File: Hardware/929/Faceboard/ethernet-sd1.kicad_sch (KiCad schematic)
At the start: 13 parts, among them J2 Raspberry_Pi_to_Ziloo, J4 RJ45_LED_Shielded

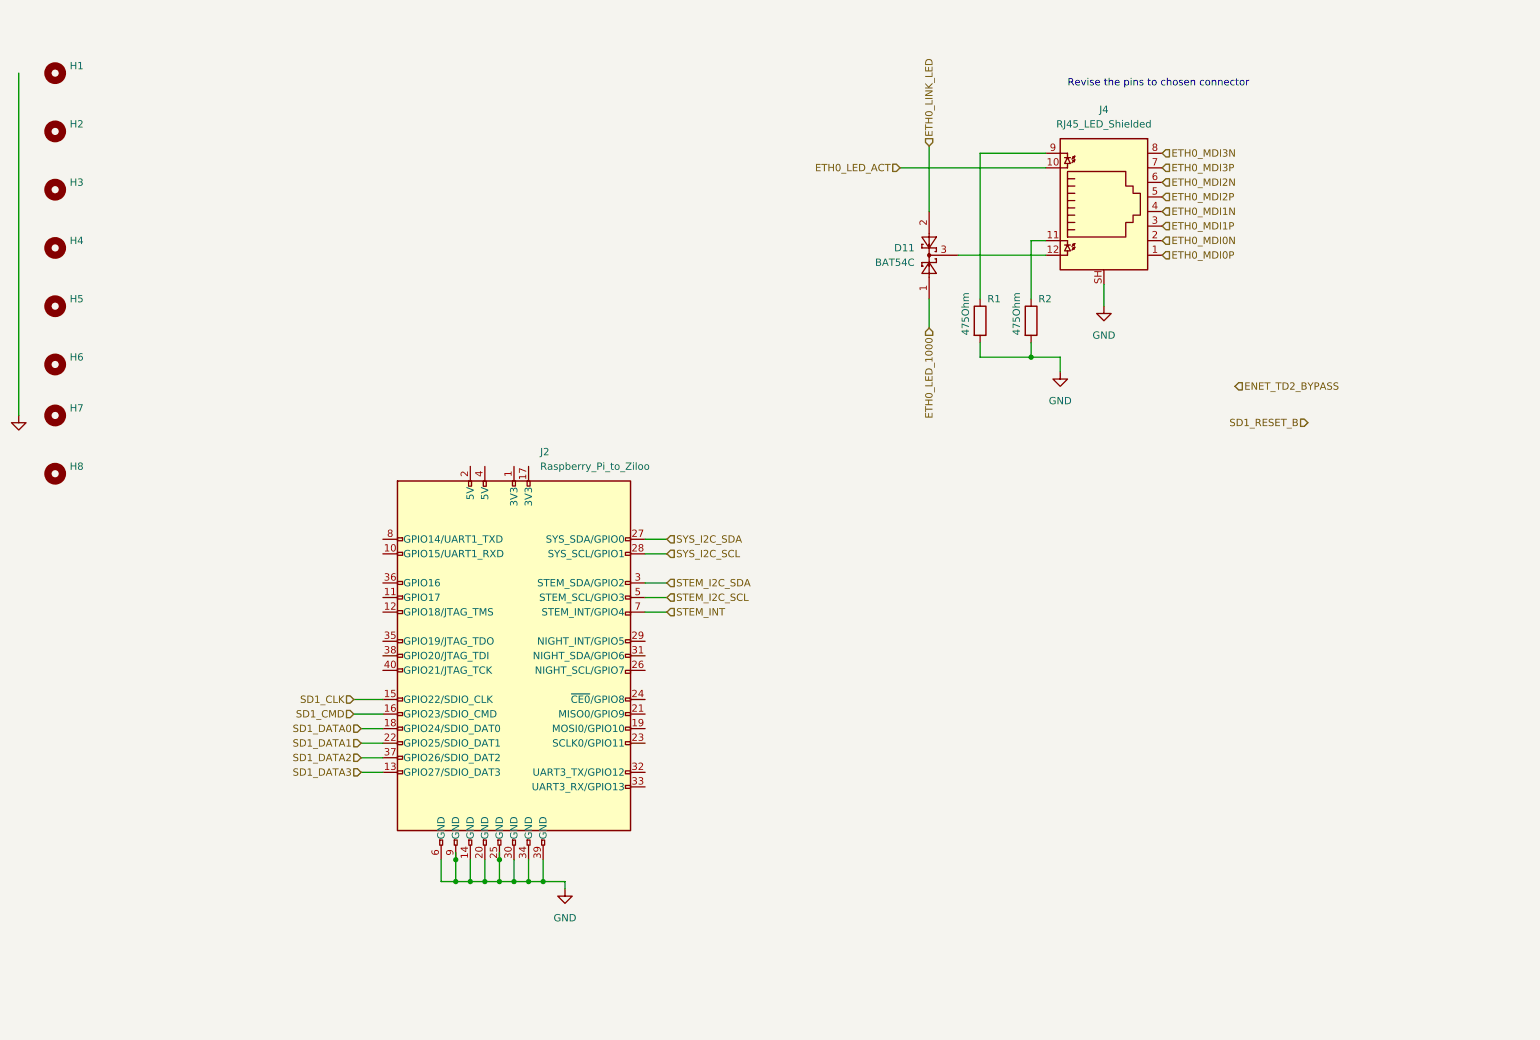
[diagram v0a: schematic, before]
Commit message: Added components
ESD HDMI
Extra components planned
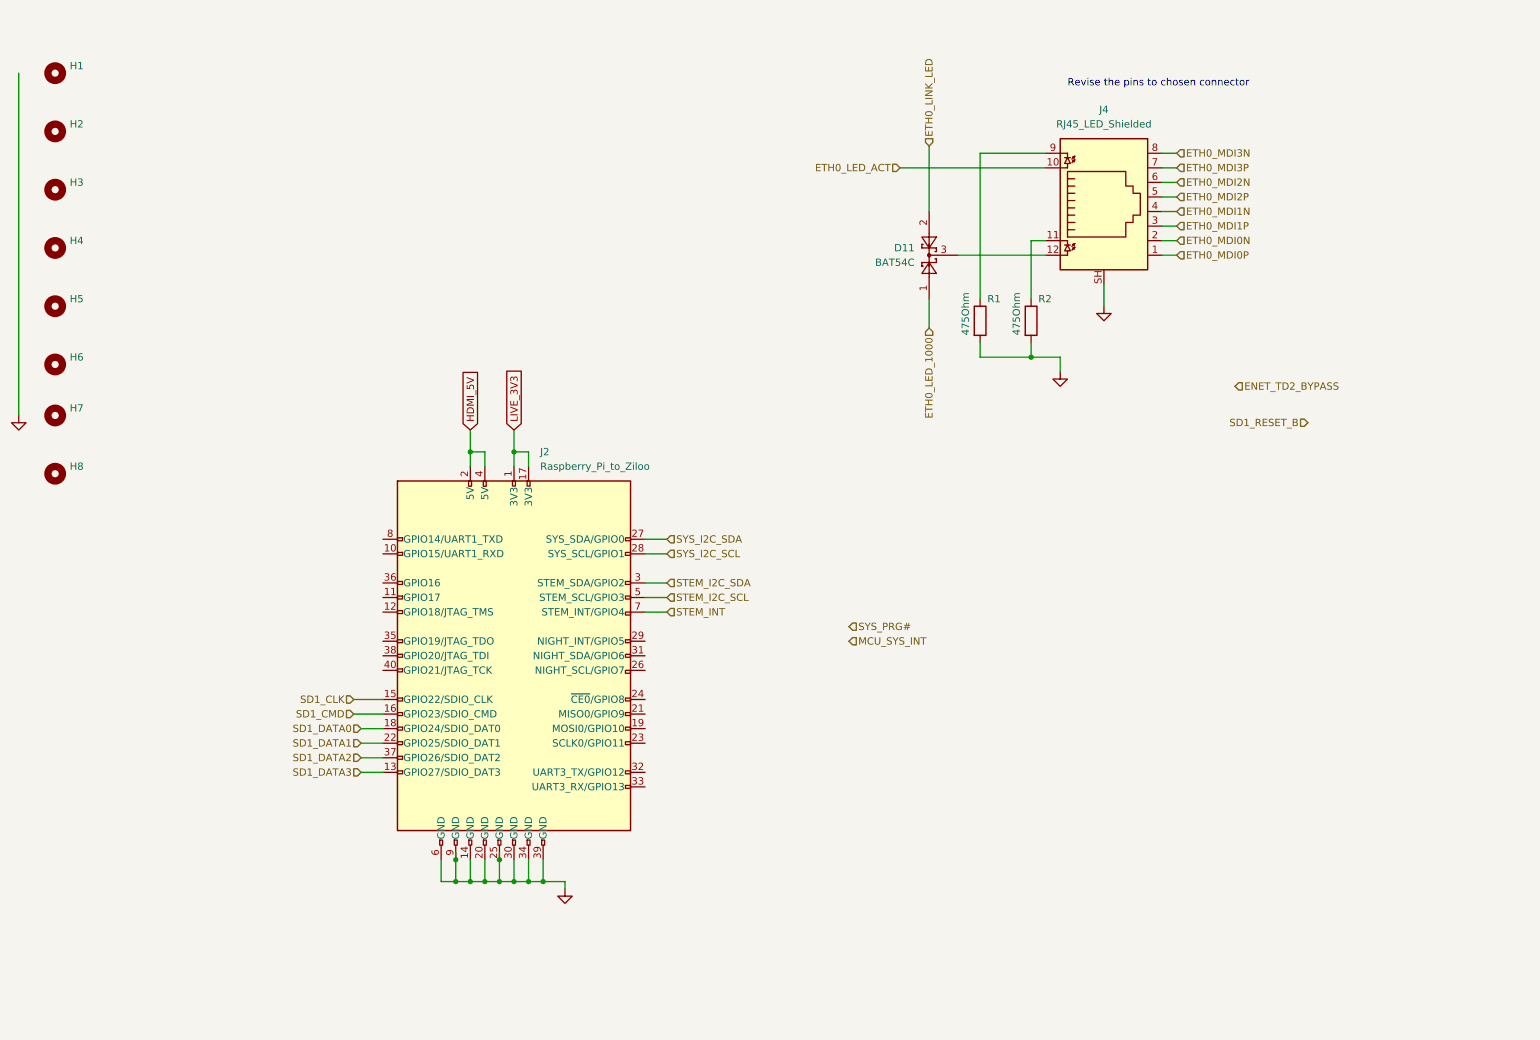
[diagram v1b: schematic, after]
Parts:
- J4: footprint (none) -> Connector_RJ:RJ45_Molex_0855135013_Vertical
- R1, R2: footprint (none) -> Resistor_SMD:R_0402_1005Metric
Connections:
- net LIVE_3V3: now reaches J2.1 (3V3)
- net LIVE_3V3: now also J2.17 (3V3)
- net HDMI_5V: now reaches J2.2 (5V)
- net HDMI_5V: now also J2.4 (5V)
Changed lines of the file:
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@@
   (junction (at 96.52 165.1) (diameter 0) (color 0 0 0 0)
   )
+  (junction (at 104.14 90.17) (diameter 0) (color 0 0 0 0)
+  )
   (junction (at 109.22 165.1) (diameter 0) (color 0 0 0 0)
   )
@@
   (junction (at 101.6 161.29) (diameter 0) (color 0 0 0 0)
   )
+  (junction (at 96.52 90.17) (diameter 0) (color 0 0 0 0)
+  )
   (junction (at 194.31 73.66) (diameter 0) (color 0 0 0 0)
   )
@@
     (stroke (width 0) (type default) (color 0 0 0 0))
   )
+  (wire (pts (xy 219.71 43.18) (xy 217.17 43.18))
+    (stroke (width 0) (type default) (color 0 0 0 0))
+  )
   (wire (pts (xy 171.45 40.64) (xy 196.85 40.64))
     (stroke (width 0) (type default) (color 0 0 0 0))
@@
     (stroke (width 0) (type default) (color 0 0 0 0))
   )
+  (wire (pts (xy 219.71 50.8) (xy 217.17 50.8))
+    (stroke (width 0) (type default) (color 0 0 0 0))
+  )
+  (wire (pts (xy 219.71 40.64) (xy 217.17 40.64))
+    (stroke (width 0) (type default) (color 0 0 0 0))
+  )
   (wire (pts (xy 93.98 165.1) (xy 91.44 165.1))
     (stroke (width 0) (type default) (color 0 0 0 0))
@@
     (stroke (width 0) (type default) (color 0 0 0 0))
   )
+  (wire (pts (xy 219.71 55.88) (xy 217.17 55.88))
+    (stroke (width 0) (type default) (color 0 0 0 0))
+  )
   (wire (pts (xy 185.42 38.1) (xy 185.42 63.5))
     (stroke (width 0) (type default) (color 0 0 0 0))
   )
+  (wire (pts (xy 99.06 90.17) (xy 96.52 90.17))
+    (stroke (width 0) (type default) (color 0 0 0 0))
+  )
   (wire (pts (xy 196.85 53.34) (xy 194.31 53.34))
     (stroke (width 0) (type default) (color 0 0 0 0))
   )
+  (wire (pts (xy 219.71 53.34) (xy 217.17 53.34))
+    (stroke (width 0) (type default) (color 0 0 0 0))
+  )
   (wire (pts (xy 199.39 73.66) (xy 199.39 76.2))
     (stroke (width 0) (type default) (color 0 0 0 0))
   )
+  (wire (pts (xy 106.68 90.17) (xy 104.14 90.17))
+    (stroke (width 0) (type default) (color 0 0 0 0))
+  )
   (wire (pts (xy 101.6 160.02) (xy 101.6 161.29))
     (stroke (width 0) (type default) (color 0 0 0 0))
@@
     (stroke (width 0) (type default) (color 0 0 0 0))
   )
+  (wire (pts (xy 219.71 45.72) (xy 217.17 45.72))
+    (stroke (width 0) (type default) (color 0 0 0 0))
+  )
+  (wire (pts (xy 96.52 86.36) (xy 96.52 90.17))
+    (stroke (width 0) (type default) (color 0 0 0 0))
+  )
   (wire (pts (xy 130.81 118.11) (xy 127 118.11))
     (stroke (width 0) (type default) (color 0 0 0 0))
@@
     (stroke (width 0) (type default) (color 0 0 0 0))
   )
+  (wire (pts (xy 106.68 92.71) (xy 106.68 90.17))
+    (stroke (width 0) (type default) (color 0 0 0 0))
+  )
+  (wire (pts (xy 104.14 90.17) (xy 104.14 92.71))
+    (stroke (width 0) (type default) (color 0 0 0 0))
+  )
   (wire (pts (xy 194.31 71.12) (xy 194.31 73.66))
     (stroke (width 0) (type default) (color 0 0 0 0))
   )
+  (wire (pts (xy 99.06 92.71) (xy 99.06 90.17))
+    (stroke (width 0) (type default) (color 0 0 0 0))
+  )
   (wire (pts (xy 106.68 165.1) (xy 104.14 165.1))
     (stroke (width 0) (type default) (color 0 0 0 0))
   )
+  (wire (pts (xy 96.52 90.17) (xy 96.52 92.71))
+    (stroke (width 0) (type default) (color 0 0 0 0))
+  )
+  (wire (pts (xy 219.71 48.26) (xy 217.17 48.26))
+    (stroke (width 0) (type default) (color 0 0 0 0))
+  )
   (wire (pts (xy 76.2 135.89) (xy 81.28 135.89))
     (stroke (width 0) (type default) (color 0 0 0 0))
@@
     (stroke (width 0) (type default) (color 0 0 0 0))
   )
+  (wire (pts (xy 104.14 86.36) (xy 104.14 90.17))
+    (stroke (width 0) (type default) (color 0 0 0 0))
+  )
   (wire (pts (xy 77.47 140.97) (xy 81.28 140.97))
+    (stroke (width 0) (type default) (color 0 0 0 0))
+  )
+  (wire (pts (xy 219.71 38.1) (xy 217.17 38.1))
     (stroke (width 0) (type default) (color 0 0 0 0))
   )
@@
     (effects (font (size 1.27 1.27)) (justify left bottom))
   )
-  (hierarchical_label "ETH0_MDI0N" (shape input) (at 217.17 53.34 0)
+  (global_label "LIVE_3V3" (shape input) (at 104.14 86.36 90) (fields_autoplaced)
+    (effects (font (size 1.27 1.27)) (justify left))
+    (property "Intersheet References" "${INTERSHEET_REFS}" (id 0) (at 104.0606 75.6012 90)
+      (effects (font (size 1.27 1.27)) (justify left) hide)
+    )
+  )
+  (global_label "HDMI_5V" (shape input) (at 96.52 86.36 90) (fields_autoplaced)
+    (effects (font (size 1.27 1.27)) (justify left))
+    (property "Intersheet References" "${INTERSHEET_REFS}" (id 0) (at 96.4406 76.0245 90)
+      (effects (font (size 1.27 1.27)) (justify left) hide)
+    )
+  )
+  (hierarchical_label "ETH0_MDI0N" (shape input) (at 219.71 53.34 0)
     (effects (font (size 1.27 1.27)) (justify left))
   )
@@
     (effects (font (size 1.27 1.27)) (justify right))
   )
-  (hierarchical_label "ETH0_MDI3N" (shape input) (at 217.17 38.1 0)
+  (hierarchical_label "ETH0_MDI3N" (shape input) (at 219.71 38.1 0)
     (effects (font (size 1.27 1.27)) (justify left))
   )
@@
     (effects (font (size 1.27 1.27)) (justify right))
   )
-  (hierarchical_label "ETH0_MDI2N" (shape input) (at 217.17 43.18 0)
-    (effects (font (size 1.27 1.27)) (justify left))
-  )
-  (hierarchical_label "ETH0_MDI3P" (shape input) (at 217.17 40.64 0)
-    (effects (font (size 1.27 1.27)) (justify left))
-  )
-  (hierarchical_label "ETH0_MDI1P" (shape input) (at 217.17 50.8 0)
+  (hierarchical_label "ETH0_MDI2N" (shape input) (at 219.71 43.18 0)
+    (effects (font (size 1.27 1.27)) (justify left))
+  )
+  (hierarchical_label "ETH0_MDI3P" (shape input) (at 219.71 40.64 0)
+    (effects (font (size 1.27 1.27)) (justify left))
+  )
+  (hierarchical_label "ETH0_MDI1P" (shape input) (at 219.71 50.8 0)
     (effects (font (size 1.27 1.27)) (justify left))
   )
@@
     (effects (font (size 1.27 1.27)) (justify left))
   )
+  (hierarchical_label "MCU_SYS_INT" (shape input) (at 162.56 123.19 0)
+    (effects (font (size 1.27 1.27)) (justify left))
+  )
   (hierarchical_label "SD1_DATA0" (shape input) (at 77.47 138.43 180)
     (effects (font (size 1.27 1.27)) (justify right))
@@
     (effects (font (size 1.27 1.27)) (justify left))
   )
+  (hierarchical_label "SYS_PRG#" (shape input) (at 162.56 120.65 0)
+    (effects (font (size 1.27 1.27)) (justify left))
+  )
   (hierarchical_label "SYS_I2C_SCL" (shape input) (at 130.81 107.95 0)
     (effects (font (size 1.27 1.27)) (justify left))
@@
     (effects (font (size 1.27 1.27)) (justify left))
   )
-  (hierarchical_label "ETH0_MDI2P" (shape input) (at 217.17 45.72 0)
-    (effects (font (size 1.27 1.27)) (justify left))
-  )
-  (hierarchical_label "ETH0_MDI0P" (shape input) (at 217.17 55.88 0)
+  (hierarchical_label "ETH0_MDI2P" (shape input) (at 219.71 45.72 0)
+    (effects (font (size 1.27 1.27)) (justify left))
+  )
+  (hierarchical_label "ETH0_MDI0P" (shape input) (at 219.71 55.88 0)
     (effects (font (size 1.27 1.27)) (justify left))
   )
@@
     (effects (font (size 1.27 1.27)) (justify left))
   )
-  (hierarchical_label "ETH0_MDI1N" (shape input) (at 217.17 48.26 0)
+  (hierarchical_label "ETH0_MDI1N" (shape input) (at 219.71 48.26 0)
     (effects (font (size 1.27 1.27)) (justify left))
   )
@@
     (property "Reference" "J4" (id 0) (at 207.01 30.48 0))
     (property "Value" "RJ45_LED_Shielded" (id 1) (at 207.01 33.02 0))
-    (property "Footprint" "" (id 2) (at 207.01 47.625 90)
+    (property "Footprint" "Connector_RJ:RJ45_Molex_0855135013_Vertical" (id 2) (at 207.01 47.625 90)
       (effects (font (size 1.27 1.27)) hide)
     )
@@
       (effects (font (size 1.27 1.27)) hide)
     )
-    (property "Value" "GND" (id 1) (at 199.39 81.28 0))
+    (property "Value" "GND" (id 1) (at 199.39 81.28 0)
+      (effects (font (size 1.27 1.27)) hide)
+    )
     (property "Footprint" "" (id 2) (at 199.39 76.2 0)
       (effects (font (size 1.27 1.27)) hide)
@@
       (effects (font (size 1.27 1.27)) hide)
     )
-    (property "Value" "GND" (id 1) (at 113.03 171.45 0))
+    (property "Value" "GND" (id 1) (at 113.03 171.45 0)
+      (effects (font (size 1.27 1.27)) hide)
+    )
     (property "Footprint" "" (id 2) (at 113.03 166.37 0)
       (effects (font (size 1.27 1.27)) hide)
@@
       (effects (font (size 1.27 1.27)) hide)
     )
-    (property "Value" "GND" (id 1) (at 207.01 69.85 0))
+    (property "Value" "GND" (id 1) (at 207.01 69.85 0)
+      (effects (font (size 1.27 1.27)) hide)
+    )
     (property "Footprint" "" (id 2) (at 207.01 64.77 0)
       (effects (font (size 1.27 1.27)) hide)
@@
       (effects (font (size 1.27 1.27)) (justify left))
     )
-    (property "Footprint" "" (id 2) (at 192.532 67.31 90)
+    (property "Footprint" "Resistor_SMD:R_0402_1005Metric" (id 2) (at 192.532 67.31 90)
       (effects (font (size 1.27 1.27)) hide)
     )
@@
       (effects (font (size 1.27 1.27)) (justify left))
     )
-    (property "Footprint" "" (id 2) (at 183.642 67.31 90)
-      (effects (font (size 1.27 1.27)) hide)
-    )
+    (property "Footprint" "Resistor_SMD:R_0402_1005Metric" (id 2) (at 183.642 67.31 90)
+      (effects (font (size 1.27 1.27)) hide)
+    )

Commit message: Removed VSOM diodes
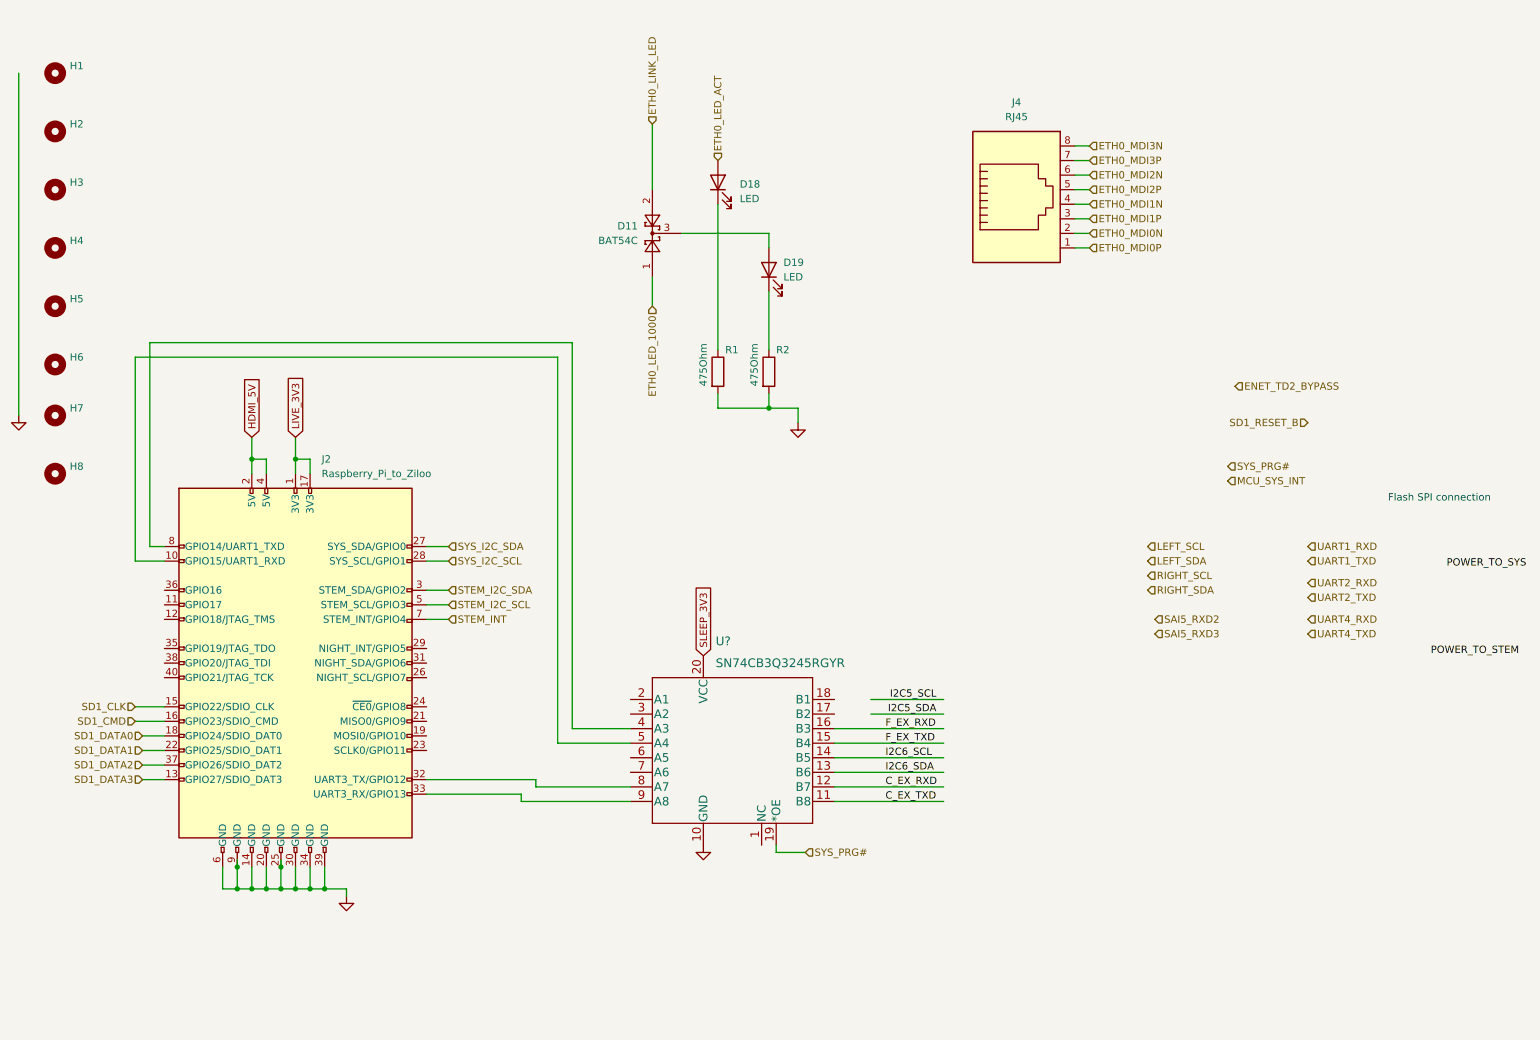
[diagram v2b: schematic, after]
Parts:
- removed J4: RJ45_LED_Shielded, Connector_RJ:RJ45_Molex_0855135013_Vertical, symbol Connector:RJ45_LED_Shielded
- added D18, D19: LED, LED_SMD:LED_0805_2012Metric, symbol Device:LED
- added J4: RJ45, Connector_RJ:RJ45_Molex_0855135013_Vertical, symbol Connector:RJ45
- added U?: SN74CB3Q3245RGYR, Ziloo:SN74CB3Q3245RGYR, symbol Ziloo:SN74CB3Q3245PW
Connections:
- net ETH0_LED_ACT: now also D18.2 (A)
- net ETH0_MDI0N: now also J4.2
- net ETH0_MDI0P: now also J4.1
- net ETH0_MDI1N: now also J4.4
- net ETH0_MDI1P: now also J4.3
- net ETH0_MDI2N: now also J4.6
- net ETH0_MDI2P: now also J4.5
- net ETH0_MDI3N: now also J4.8
- net ETH0_MDI3P: now also J4.7
- net GND: now also U?.10 (GND)
- net SYS_PRG#: now also U?.19 (*OE)
- net at D11.3: now also D19.2 (A)
- net at J2.10 (GPIO15/UART1_RXD): now also U?.5 (A4)
- net at J2.32 (UART3_TX/GPIO12): now also U?.8 (A7)
- net at J2.33 (UART3_RX/GPIO13): now also U?.9 (A8)
- net at J2.8 (GPIO14/UART1_TXD): now also U?.4 (A3)
- net at R2.1: now also D19.1 (K)
- net at R1.1: now also D18.1 (K)
- new net C_EX_RXD: U?.12 (B7)
- new net C_EX_TXD: U?.11 (B8)
- new net F_EX_RXD: U?.16 (B3)
- new net F_EX_TXD: U?.15 (B4)
- new net I2C6_SCL: U?.14 (B5)
- new net I2C6_SDA: U?.13 (B6)
- new net SLEEP_3V3: U?.20 (VCC)
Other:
- note added: "Flash SPI connection"
- note removed: "Revise the pins to chosen connector"
- moved on the sheet: J2, R1, R2
